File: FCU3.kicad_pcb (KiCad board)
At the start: 6 copper layers, 0 parts

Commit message: Attempt 3 to fix logo
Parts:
- added C1: 1uF, Capacitor_SMD:C_0603_1608Metric_Pad1.08x0.95mm_HandSolder, F.Cu at (130.2, 73.4)
- added C10: 10uF, Capacitor_SMD:C_0603_1608Metric_Pad1.08x0.95mm_HandSolder, F.Cu at (166.5, 122.4)
- added C11: 10uF, Capacitor_SMD:C_0603_1608Metric_Pad1.08x0.95mm_HandSolder, F.Cu at (130.2, 78.4)
- added C12: 100nF, Capacitor_SMD:C_0603_1608Metric_Pad1.08x0.95mm_HandSolder, F.Cu at (170.9, 114.9)
- added C13: 100nF, Capacitor_SMD:C_0603_1608Metric_Pad1.08x0.95mm_HandSolder, F.Cu at (123.1, 104.0)
- added C14: 100nF, Capacitor_SMD:C_0603_1608Metric_Pad1.08x0.95mm_HandSolder, F.Cu at (123.1, 106.5)
- added C15: 27pF, Capacitor_SMD:C_0603_1608Metric_Pad1.08x0.95mm_HandSolder, F.Cu at (170.9, 117.4)
- added C16: 27pF, Capacitor_SMD:C_0603_1608Metric_Pad1.08x0.95mm_HandSolder, F.Cu at (170.9, 119.9)
- added C17: 100nF, Capacitor_SMD:C_0603_1608Metric_Pad1.08x0.95mm_HandSolder, F.Cu at (123.1, 109.0)
- added C18: 100nF, Capacitor_SMD:C_0603_1608Metric_Pad1.08x0.95mm_HandSolder, F.Cu at (130.2, 80.9)
- added C19: 10uF, Capacitor_SMD:C_1206_3216Metric, F.Cu at (135.2, 73.8)
- added C2: 1uF, Capacitor_SMD:C_0603_1608Metric_Pad1.08x0.95mm_HandSolder, F.Cu at (130.2, 75.9)
- added C20: 10uF, Capacitor_SMD:C_1206_3216Metric, F.Cu at (135.2, 77.2)
- added C21: 10uF, Capacitor_SMD:C_1206_3216Metric, F.Cu at (135.2, 80.5)
- added C22: 10uF, Capacitor_SMD:C_1206_3216Metric, F.Cu at (135.2, 83.9)
- added C23: 10uF, Capacitor_SMD:C_1206_3216Metric, F.Cu at (135.2, 87.2)
- added C3: 100nF, Capacitor_SMD:C_0603_1608Metric_Pad1.08x0.95mm_HandSolder, F.Cu at (162.2, 114.9)
- added C4: 100nF, Capacitor_SMD:C_0603_1608Metric_Pad1.08x0.95mm_HandSolder, F.Cu at (162.2, 117.4)
- added C5: 100nF, Capacitor_SMD:C_0603_1608Metric_Pad1.08x0.95mm_HandSolder, F.Cu at (162.2, 119.9)
- added C6: 100nF, Capacitor_SMD:C_0603_1608Metric_Pad1.08x0.95mm_HandSolder, F.Cu at (162.2, 122.4)
- added C7: 2.2uF, Capacitor_SMD:C_0603_1608Metric_Pad1.08x0.95mm_HandSolder, F.Cu at (166.5, 114.9)
- added C8: 2.2uF, Capacitor_SMD:C_0603_1608Metric_Pad1.08x0.95mm_HandSolder, F.Cu at (166.5, 117.4)
- added C9: 2.2uF, Capacitor_SMD:C_0603_1608Metric_Pad1.08x0.95mm_HandSolder, F.Cu at (166.5, 119.9)
- added D1: SS14, Diode_SMD:D_SMA, F.Cu at (136.5, 91.2)
- added D2: SS14, Diode_SMD:D_SMA, F.Cu at (136.5, 95.7)
- added H1: MountingHole_Pad_MP, MountingHole:MountingHole_3.2mm_M3_DIN965_Pad, F.Cu at (124.5, 75.7)
- added H2: MountingHole_Pad_MP, MountingHole:MountingHole_3.2mm_M3_DIN965_Pad, F.Cu at (124.5, 82.9)
- added H3: MountingHole_Pad_MP, MountingHole:MountingHole_3.2mm_M3_DIN965_Pad, F.Cu at (124.5, 90.0)
- added H4: MountingHole_Pad_MP, MountingHole:MountingHole_3.2mm_M3_DIN965_Pad, F.Cu at (124.5, 97.2)
- added J1: SM06B-SRSS-TB_LF__SN_, KSE_connector:JST_SM06B-SRSS-TB_LF__SN_, F.Cu at (156.4, 83.7)
- added J2: SM06B-SRSS-TB_LF__SN_, KSE_connector:JST_SM06B-SRSS-TB_LF__SN_, F.Cu at (156.4, 90.8)
- added J4: SM08B-SRSS-TB_LF__SN_, KSE_connector:JST_SM08B-SRSS-TB_LF__SN_, F.Cu at (167.7, 88.4)
- added J6: UJ20-C-H-G-SMT-1-P16-TR, KSE_connector:SAMESKY_UJ20-C-H-G-SMT-1-P16-TR, F.Cu at (152.5, 81.3)
- added JP3: SolderJumper_2_Bridged, Jumper:SolderJumper-2_P1.3mm_Bridged2Bar_Pad1.0x1.5mm, F.Cu at (142.7, 90.7)
- added JP4: SolderJumper_2_Bridged, Jumper:SolderJumper-2_P1.3mm_Bridged2Bar_Pad1.0x1.5mm, F.Cu at (142.7, 94.2)
- added PS1: TPSM84338RCJR, KSE_DCDC:TPSM84338RCJR, F.Cu at (141.3, 75.4)
- added Q2: SS8050, Package_TO_SOT_SMD:SOT-23, F.Cu at (168.8, 91.6)
- added R1: 75k, Resistor_SMD:R_0603_1608Metric_Pad0.98x0.95mm_HandSolder, F.Cu at (149.0, 83.4)
- added R10: 4.7k, Resistor_SMD:R_0603_1608Metric_Pad0.98x0.95mm_HandSolder, F.Cu at (149.0, 95.9)
- added R11: 10k, Resistor_SMD:R_0603_1608Metric_Pad0.98x0.95mm_HandSolder, F.Cu at (130.2, 88.5)
- added R15: 5.1k, Resistor_SMD:R_0805_2012Metric_Pad1.20x1.40mm_HandSolder, F.Cu at (163.9, 93.6)
- added R2: 10k, Resistor_SMD:R_0603_1608Metric_Pad0.98x0.95mm_HandSolder, F.Cu at (149.0, 85.9)
- added R3: 10k, Resistor_SMD:R_0603_1608Metric_Pad0.98x0.95mm_HandSolder, F.Cu at (149.0, 88.4)
- added R4: 1k, Resistor_SMD:R_0603_1608Metric_Pad0.98x0.95mm_HandSolder, F.Cu at (149.0, 90.9)
- added R5: 18k, Resistor_SMD:R_0603_1608Metric_Pad0.98x0.95mm_HandSolder, F.Cu at (130.2, 83.4)
- added R6: 140k, Resistor_SMD:R_0603_1608Metric_Pad0.98x0.95mm_HandSolder, F.Cu at (130.2, 85.9)
- added R7: 4.7k, Resistor_SMD:R_0603_1608Metric_Pad0.98x0.95mm_HandSolder, F.Cu at (149.0, 93.4)
- added R8: 10k, Resistor_SMD:R_0603_1608Metric_Pad0.98x0.95mm_HandSolder, F.Cu at (170.9, 122.4)
- added R9: 5.1k, Resistor_SMD:R_0805_2012Metric_Pad1.20x1.40mm_HandSolder, F.Cu at (163.9, 90.6)
- added S1: TS32-7-35-BK-B-260-RA-SMT-TR, KSE_sensor:SW_TS32-7-35-BK-B-260-RA-SMT-TR, F.Cu at (166.3, 101.8)
- added U1: MPU-6500, KSE_sensor:QFN40P300X300X95-25N, F.Cu at (128.4, 105.4)
- added U3: MCP1700x-330xxTT, Package_TO_SOT_SMD:SOT-23, F.Cu at (140.5, 80.8)
- added U5: STM32F405RGTx, Package_QFP:LQFP-64_10x10mm_P0.5mm, F.Cu at (154.1, 106.4)
- added Y1: LFXTAL055207Bulk, KSE_passive:Crystal_HC49-4H_Vertical, F.Cu at (151.0, 116.9)

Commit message: Start of layout
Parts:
- moved U3 93.5 mm to (53.2, 47.3)
- moved D1 93.5 mm to (49.2, 57.7)
- moved D2 93.5 mm to (49.2, 62.3)
- moved PS1 93.5 mm to (54.0, 41.9)
- moved Y1 93.5 mm to (63.7, 83.5)
- moved C1 93.5 mm to (43.0, 39.9)
- moved C10 93.5 mm to (79.2, 88.9)
- moved C11 93.5 mm to (43.0, 45.0)
- moved C12 93.5 mm to (83.6, 81.4)
- moved C13 93.5 mm to (35.8, 70.5)
- moved C14 93.5 mm to (35.8, 73.0)
- moved C15 93.5 mm to (83.6, 83.9)
- moved C16 93.5 mm to (83.6, 86.4)
- moved C17 93.5 mm to (35.8, 75.6)
- moved C18 93.5 mm to (43.0, 47.5)
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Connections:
- J2 pad 1: DGND -> /Project Architecture/UART5_RX
- J2 pad 2: +3V3 -> /Project Architecture/UART5_TX
- J2 pad 3: /Project Architecture/UART5_RX -> DGND
- J2 pad 4: /Project Architecture/UART5_TX -> +3V3
- U5 pad 53: /Project Architecture/UART5_RX -> /Project Architecture/UART5_TX
- U5 pad 54: /Project Architecture/UART5_TX -> /Project Architecture/UART5_RX
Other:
- board outline added: 36.7 x 36.7 mm

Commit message: Layout half-way done.
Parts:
- C1, C11, C18, C19, C2, C20, C21, C22, C23, JP3, JP4, PS1, Q2, R1, R10, R11, R15, R2, R3, R4, R5, R6, R7, R8, R9, U3, Y1: moved to B.Cu
- moved C1 109.1 mm to (116.5, 120.5), turned to -90 degrees
- moved C11 109.0 mm to (124.4, 117.3), turned to 180 degrees
- moved C18 108.4 mm to (124.4, 118.9), turned to 180 degrees
- moved D1 104.3 mm to (125.3, 129.0), turned to 90 degrees
- moved R5 104.2 mm to (121.7, 118.2), turned to 90 degrees
- moved C2 103.6 mm to (111.0, 120.5), turned to -90 degrees
- moved R6 100.1 mm to (119.0, 117.5)
- moved PS1 99.7 mm to (123.0, 113.8)
- moved R3 97.8 mm to (130.2, 124.8), turned to 180 degrees
- moved R11 97.5 mm to (119.0, 115.9), turned to 180 degrees
- moved JP3 95.9 mm to (117.1, 130.7), turned to -90 degrees
- moved C19 95.3 mm to (109.9, 112.7), turned to -90 degrees
- moved U3 95.0 mm to (113.7, 120.5)
- moved C20 94.4 mm to (112.3, 112.7), turned to -90 degrees
- moved C21 93.7 mm to (114.7, 112.7), turned to -90 degrees
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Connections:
- C10 pad 2: AGND -> DGND
- R10 pad 1: /Project Architecture/I2C1_SCL -> /Project Architecture/I2C1_SDA
- R10 pad 2: DGND -> +3V3
- R7 pad 1: /Project Architecture/I2C1_SDA -> /Project Architecture/I2C1_SCL
- R7 pad 2: DGND -> +3V3
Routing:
- net PGND: track 0.00 -> 56.0 mm
- net DGND: track 0.00 -> 36.4 mm, vias 0 -> 6
- net +3V3: track 0.00 -> 26.3 mm, vias 0 -> 2
- net +9V: track 0.00 -> 22.8 mm, vias 0 -> 2
- net AGND: track 0.00 -> 7.45 mm, vias 0 -> 1
- net /Project Architecture/USB_CC2: track 0.00 -> 6.79 mm, vias 0 -> 1
- net /Project Architecture/Microcontroller/DFU_Enable: track 0.00 -> 6.68 mm, vias 0 -> 2
- net /Project Architecture/USB_CC1: track 0.00 -> 6.68 mm, vias 0 -> 1
- net Net-(PS1-MODE): track 0.00 -> 6.64 mm, vias 0 -> 2
- net /Project Architecture/V_USB: track 0.00 -> 6.64 mm
- net /Project Architecture/I2C1_SCL: track 0.00 -> 6.52 mm, vias 0 -> 1
- net +VBAT: track 0.00 -> 6.37 mm, vias 0 -> 1
- net /Project Architecture/I2C1_SDA: track 0.00 -> 5.75 mm, vias 0 -> 1
- net /Project Architecture/SBUS_TX: track 0.00 -> 5.49 mm, vias 0 -> 1
- net /Project Architecture/Microcontroller/CLK_OUT: track 0.00 -> 4.37 mm
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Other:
- copper layers 6 -> 4

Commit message: Floor Plan Complete
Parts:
- moved R10 70.6 mm to (163.2, 80.3), turned to 180 degrees
- moved R7 69.3 mm to (163.2, 82.0), turned to 180 degrees
- moved J2 63.5 mm to (160.8, 83.5), turned to 90 degrees
- moved JP4 54.6 mm to (148.7, 80.8)
- moved C2 52.8 mm to (146.2, 81.2), turned to 90 degrees
- moved U3 49.3 mm to (143.4, 81.2), turned to 180 degrees
- moved U1 49.3 mm to (160.8, 98.7), turned to 180 degrees
- moved D1 48.3 mm to (137.7, 82.3), turned to -90 degrees
- moved C13 48.0 mm to (161.9, 94.7), turned to 90 degrees
- moved C1 46.2 mm to (140.7, 81.2), turned to 90 degrees
- moved C17 45.8 mm to (160.2, 94.7), turned to 90 degrees
- moved C14 45.8 mm to (157.9, 98.7), turned to -90 degrees
- moved R15 44.1 mm to (144.1, 73.6)
- moved R9 44.1 mm to (146.1, 73.6)
- moved J6 44.1 mm to (145.0, 71.4)
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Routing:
- net /Project Architecture/V_USB: track 6.64 -> 17.6 mm
- net +9V: track 22.8 -> 29.6 mm, vias 2 -> 5
- net Net-(D1-K): track 2.16 -> 7.78 mm, vias 0 -> 3
- net Net-(PS1-MODE): track 6.64 -> 1.85 mm
- net PGND: track 56.0 -> 53.3 mm
- net DGND: track 36.4 -> 33.8 mm
- net /Project Architecture/USB_CC1: track 6.68 -> 4.30 mm
- net /Project Architecture/USB_CC2: track 6.79 -> 4.45 mm
- added copper zone on F.Cu, net +9V
- added copper zone on In1.Cu, net DGND
- added copper zone on In2.Cu, net PGND

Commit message: Initial Wiring Complete
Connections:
- U1 pad 23: /Project Architecture/Inertial Measurement Unit/SPI1_SCK -> /Project Architecture/SPI1_SCK
- U1 pad 24: /Project Architecture/Inertial Measurement Unit/SPI1_SDO -> /Project Architecture/SPI1_SDO
- U1 pad 9: /Project Architecture/Inertial Measurement Unit/SPI1_SDI -> /Project Architecture/SPI1_SDI
- U5 pad 21: /Project Architecture/Microcontroller/SPI1_SCK -> /Project Architecture/SPI1_SCK
- U5 pad 22: /Project Architecture/Microcontroller/SPI1_SDI -> /Project Architecture/SPI1_SDI
- U5 pad 23: /Project Architecture/Microcontroller/SPI1_SDO -> /Project Architecture/SPI1_SDO
- U5 pad 61: /Project Architecture/Microcontroller/I2C1_SCL -> /Project Architecture/I2C1_SCL
- U5 pad 62: /Project Architecture/Microcontroller/I2C1_SDA -> /Project Architecture/I2C1_SDA
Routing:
- net AGND: track 7.45 -> 38.9 mm
- net /Project Architecture/UART2_RX: track 2.66 -> 32.2 mm, vias 0 -> 3
- net /Project Architecture/UART4_TX: track 0.00 -> 28.0 mm, vias 0 -> 3
- net /Project Architecture/UART4_RX: track 0.00 -> 26.9 mm, vias 0 -> 1
- net /Project Architecture/ANA_ADC_VBAT: track 0.00 -> 26.0 mm, vias 0 -> 1
- net /Project Architecture/ESC_SIG_M3: track 0.00 -> 22.1 mm, vias 0 -> 2
- net /Project Architecture/ESC_SIG_M4: track 0.00 -> 19.5 mm, vias 0 -> 2
- net /Project Architecture/ANA_ADC_CURR: track 0.00 -> 18.0 mm, vias 0 -> 2
- net /Project Architecture/ESC_SIG_M1: track 0.00 -> 17.9 mm, vias 0 -> 2
- net DGND: track 33.8 -> 50.0 mm, vias 6 -> 10
- net /Project Architecture/SPI1_SCK: track 0.00 -> 16.1 mm
- net /Project Architecture/ESC_SIG_M2: track 0.00 -> 15.5 mm, vias 0 -> 2
- net /Project Architecture/UART1_RX: track 0.00 -> 15.2 mm, vias 0 -> 2
- net +3V3: track 26.3 -> 40.9 mm, vias 2 -> 4
- net /Project Architecture/DIG_IMU_CS: track 0.00 -> 14.0 mm
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
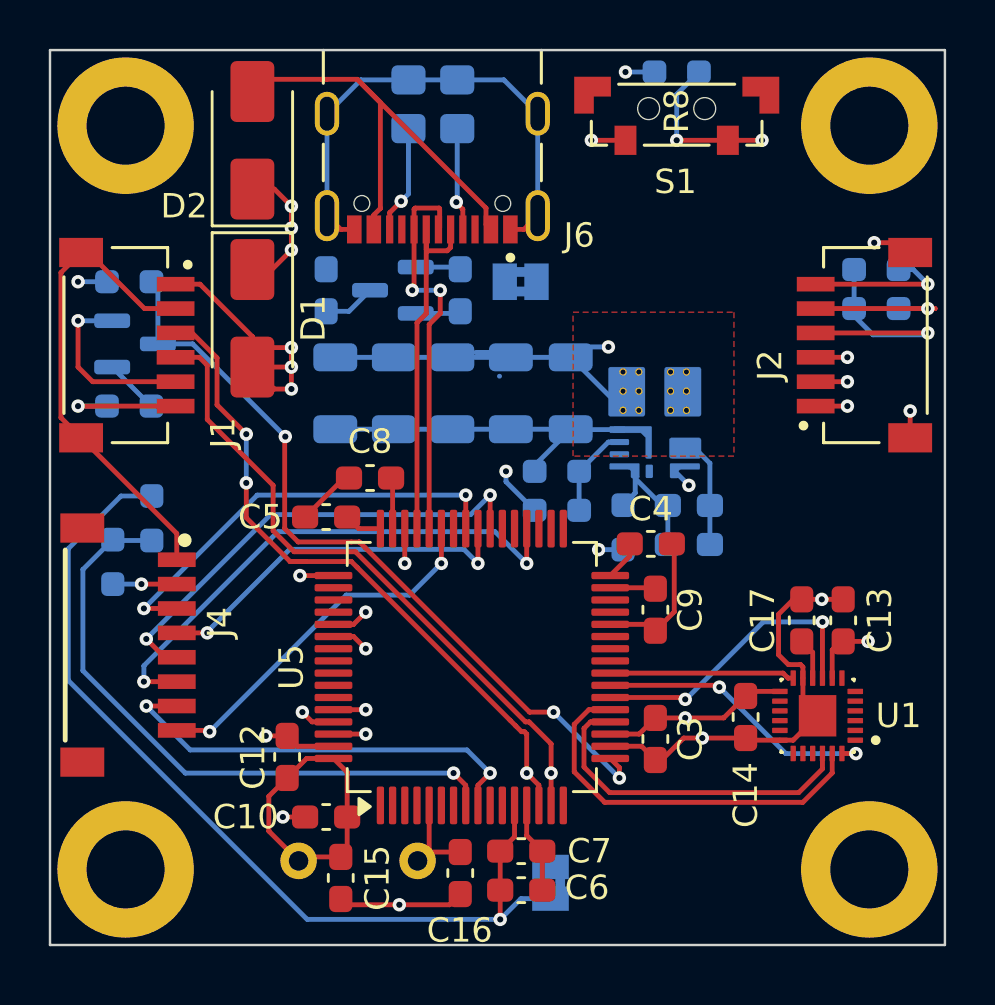
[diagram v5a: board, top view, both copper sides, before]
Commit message: Wiring Complete, ERC and DRC remaining
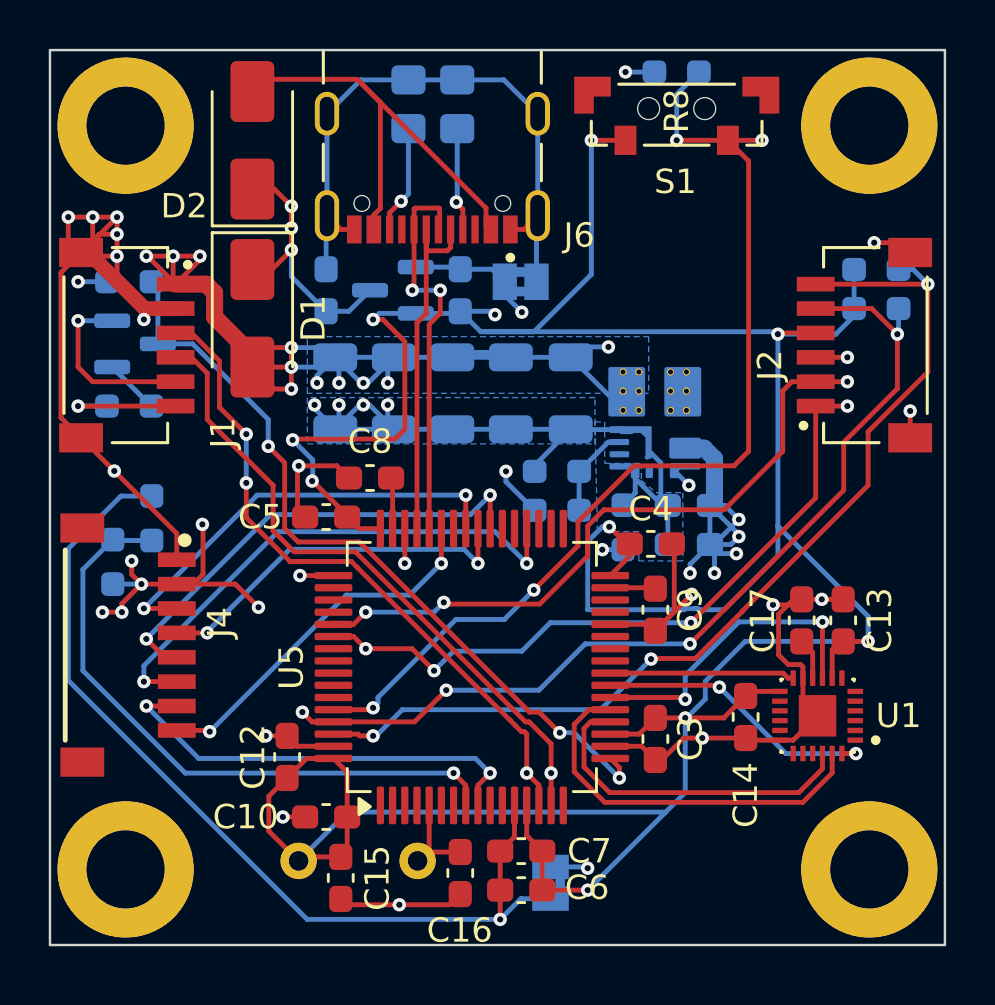
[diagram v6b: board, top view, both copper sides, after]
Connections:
- C2 pad 1: +3.3V -> +3V3
- U3 pad 2: +3.3V -> +3V3
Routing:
- net +3V3: track 40.9 -> 146.6 mm, vias 4 -> 10
- net /Project Architecture/I2C1_SDA: track 5.75 -> 41.2 mm, vias 2 -> 3
- net /Project Architecture/Microcontroller/DFU_Enable: track 8.00 -> 41.9 mm, vias 3 -> 4
- net PGND: track 60.0 -> 92.4 mm, vias 0 -> 11
- net /Project Architecture/I2C1_SCL: track 6.52 -> 38.2 mm, vias 2 -> 4
- net /Project Architecture/UART5_RX: track 2.83 -> 28.4 mm, vias 2 -> 4
- net /Project Architecture/UART5_TX: track 2.83 -> 27.4 mm, vias 2 -> 3
- net +9V: track 29.6 -> 54.1 mm, vias 5 -> 12
- net +VBAT: track 7.47 -> 28.4 mm, vias 1 -> 11
- net DGND: track 50.0 -> 60.9 mm, vias 10 -> 15
- net Net-(PS1-MODE): track 1.85 -> 7.84 mm
- net Net-(D1-K): track 7.78 -> 10.9 mm
- net (no net): track 2.77 -> 0.00 mm
- net +3.3V: track 3.05 -> 1.19 mm
- net /Project Architecture/SPI1_SDI: track 12.4 -> 12.9 mm
- added copper zone on B.Cu, net +9V
- added copper zone on In2.Cu, net +9V
- added copper zone on In2.Cu, net +VBAT
- added copper zone on B.Cu, net PGND
- removed copper zone on F.Cu, net +9V

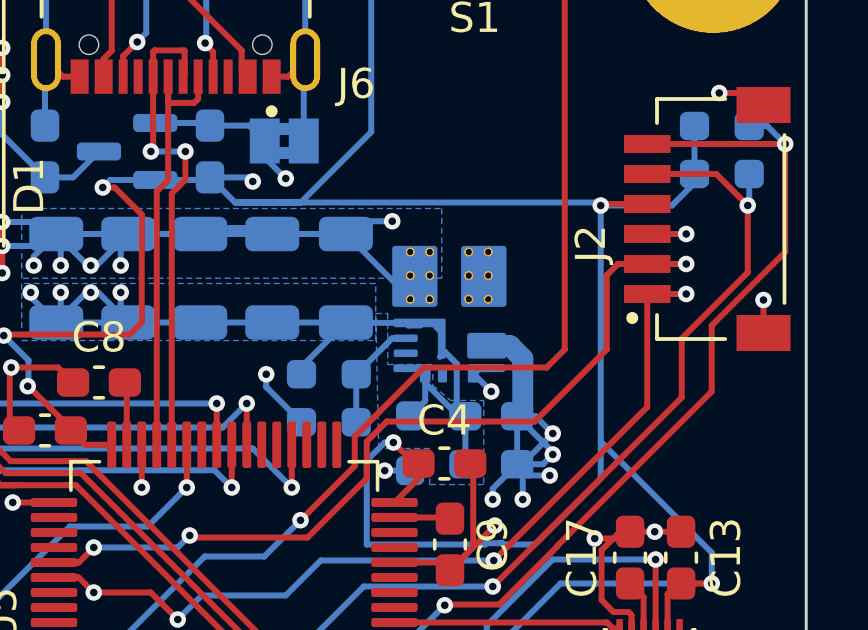
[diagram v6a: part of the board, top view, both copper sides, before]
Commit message: Modularized BEC and fixed generic components in schematic.
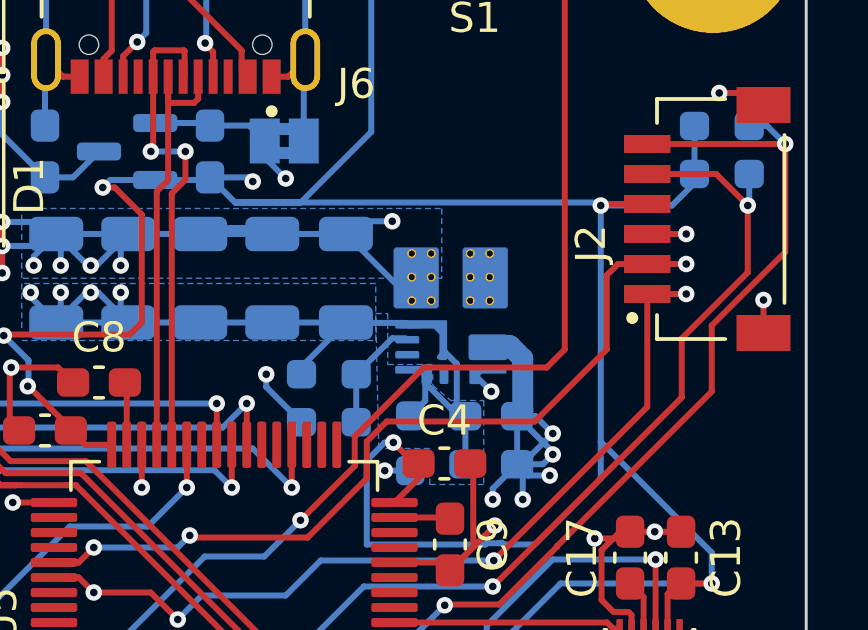
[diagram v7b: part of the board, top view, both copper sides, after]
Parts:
- moved PS1 0.07 mm to (154.2, 86.5)
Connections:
- net /Project Architecture/ANA_ADC_CURR renamed /(lib_symbols/ANA_ADC_CURR
- net /Project Architecture/ANA_ADC_VBAT renamed /(lib_symbols/ANA_ADC_VBAT
- net /Project Architecture/DIG_IMU_CS renamed /(lib_symbols/DIG_IMU_CS
- net /Project Architecture/DIG_IMU_EXTI renamed /(lib_symbols/DIG_IMU_EXTI
- net /Project Architecture/ESC_SIG_M1 renamed /(lib_symbols/ESC_SIG_M1
- net /Project Architecture/ESC_SIG_M2 renamed /(lib_symbols/ESC_SIG_M2
- net /Project Architecture/ESC_SIG_M3 renamed /(lib_symbols/ESC_SIG_M3
- net /Project Architecture/ESC_SIG_M4 renamed /(lib_symbols/ESC_SIG_M4
- net /Project Architecture/I2C1_SCL renamed /(lib_symbols/I2C1_SCL
- net /Project Architecture/I2C1_SDA renamed /(lib_symbols/I2C1_SDA
- net /Project Architecture/Microcontroller/CLK_OUT renamed /(lib_symbols/Microcontroller/CLK_OUT
- net /Project Architecture/Microcontroller/DFU_Enable renamed /(lib_symbols/Microcontroller/DFU_Enable
- net /Project Architecture/Microcontroller/LED0 renamed /(lib_symbols/Microcontroller/LED0
- net /Project Architecture/Microcontroller/LED1 renamed /(lib_symbols/Microcontroller/LED1
- net /Project Architecture/SBUS_TX renamed /(lib_symbols/SBUS_TX
- net /Project Architecture/SPI1_SCK renamed /(lib_symbols/SPI1_SCK
- net /Project Architecture/SPI1_SDI renamed /(lib_symbols/SPI1_SDI
- net /Project Architecture/SPI1_SDO renamed /(lib_symbols/SPI1_SDO
- net /Project Architecture/UART1_RX renamed /(lib_symbols/UART1_RX
- net /Project Architecture/UART2_RX renamed /(lib_symbols/UART2_RX
- net /Project Architecture/UART4_RX renamed /(lib_symbols/UART4_RX
- net /Project Architecture/UART4_TX renamed /(lib_symbols/UART4_TX
- net /Project Architecture/UART5_RX renamed /(lib_symbols/UART5_RX
- net /Project Architecture/UART5_TX renamed /(lib_symbols/UART5_TX
- net /Project Architecture/USB_+DATA renamed /(lib_symbols/USB_+DATA
- net /Project Architecture/USB_-DATA renamed /(lib_symbols/USB_-DATA
- net /Project Architecture/USB_CC1 renamed /(lib_symbols/USB_CC1
- net /Project Architecture/USB_CC2 renamed /(lib_symbols/USB_CC2
- net /Project Architecture/V_USB renamed /(lib_symbols/V_USB
- R3 pad 1: +3.3V -> +3V3
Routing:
- net +3V3: track 146.6 -> 147.8 mm, vias 10 -> 11
- net +3.3V: track 1.19 -> 0.00 mm, vias 1 -> 0
